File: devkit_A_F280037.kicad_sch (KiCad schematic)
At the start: 4 parts, among them J1 DEVKIT_C2000_ROW_A, J2 DEVKIT_C2000_ROW_B, J3 JTAG_CTBP_10, U1 TMS320F280037CSPM

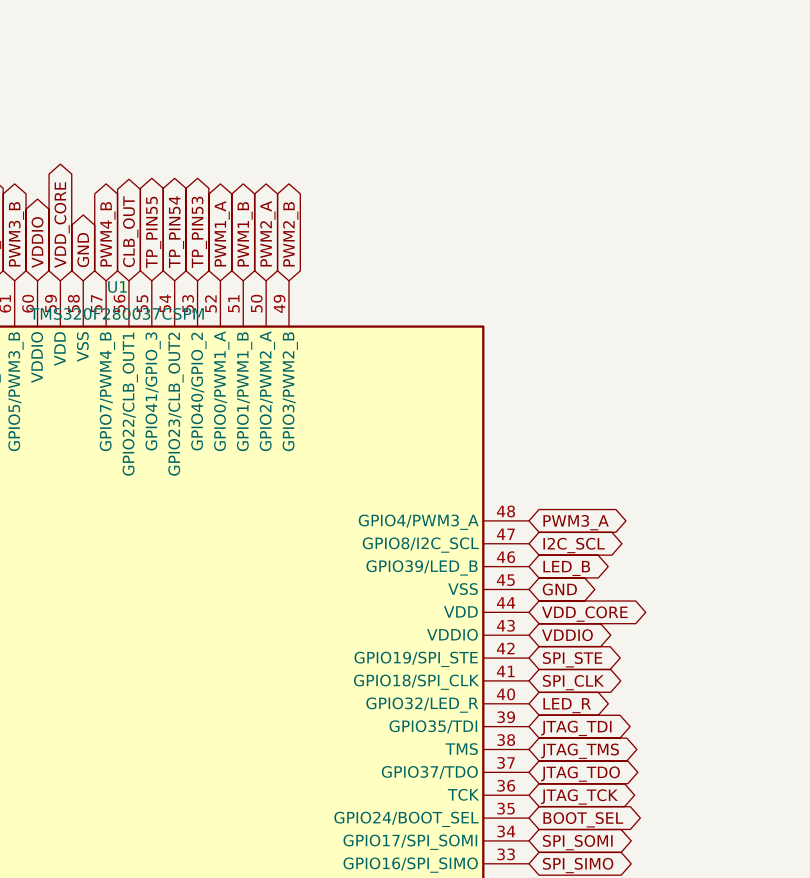
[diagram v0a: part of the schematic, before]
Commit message: LED reportees sur GPIO40 et GPIO23, les deux broches les moins dotees
GPIO32 doit valoir 1 au boot dans les deux modes retenus — Flash (1 1) et SCI
(0 1), ce dernier etant le chemin de mise a jour par l'ESP32. Une LED l'aurait
tenue vers 2,1 V, sous le VIH, cassant les deux d'un coup. GPIO39 part avec.

Broches d'accueil choisies au nombre de fonctions alternatives sacrifiees:
GPIO23 en a 7, GPIO40 en a 9, contre 12 pour GPIO9 qu'on garde libre. Elles
sont communes aux deux boitiers, donc les LED deviennent identiques sur A et B.

Les anciennes positions deviennent des pastilles, differentes par variante:
broches 46 et 40 sur le PCB A, 27 et 28 sur le PCB B.

gen_composants.py est verse au depot mais marque inutilisable: il calcule juste
et produit un fichier que KiCad refuse de charger. Cause isolee a l'insertion
des blocs lib_symbols, reproduite avec un seul Device:R et sans instance.

Co-Authored-By: Claude Opus 5 <noreply@anthropic.com>
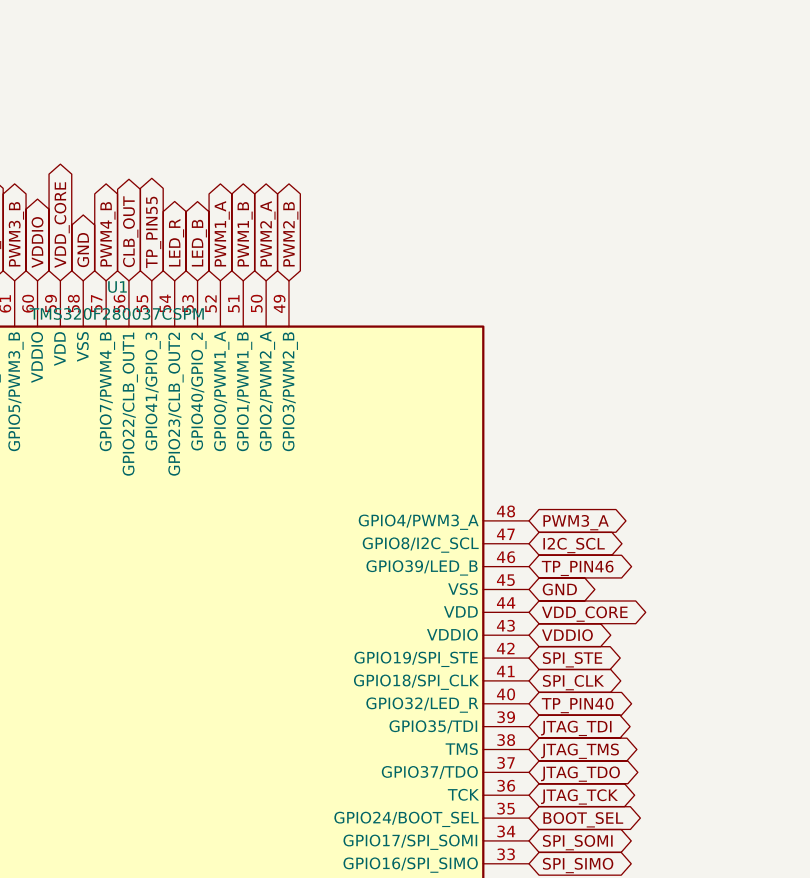
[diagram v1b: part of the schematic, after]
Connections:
- net TP_PIN53 is gone; now on net LED_B: U1.53 (GPIO40/GPIO_2)
- net TP_PIN54 is gone; now on net LED_R: U1.54 (GPIO23/CLB_OUT2)
- net LED_B: no longer U1.46 (GPIO39/LED_B)
- net LED_R: no longer U1.40 (GPIO32/LED_R)
- new net TP_PIN40: U1.40 (GPIO32/LED_R)
- new net TP_PIN46: U1.46 (GPIO39/LED_B)
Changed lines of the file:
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@@
     (effects (font (size 1.27 1.27)) (justify left))
   )
-  (global_label "LED_R" (shape bidirectional) (at 172.72 102.87 0)
+  (global_label "TP_PIN40" (shape bidirectional) (at 172.72 102.87 0)
     (effects (font (size 1.27 1.27)) (justify left))
   )
@@
     (effects (font (size 1.27 1.27)) (justify left))
   )
-  (global_label "LED_B" (shape bidirectional) (at 172.72 87.63 0)
+  (global_label "TP_PIN46" (shape bidirectional) (at 172.72 87.63 0)
     (effects (font (size 1.27 1.27)) (justify left))
   )
@@
     (effects (font (size 1.27 1.27)) (justify left))
   )
-  (global_label "TP_PIN53" (shape bidirectional) (at 135.89 55.88 90)
+  (global_label "LED_B" (shape bidirectional) (at 135.89 55.88 90)
     (effects (font (size 1.27 1.27)) (justify left))
   )
-  (global_label "TP_PIN54" (shape bidirectional) (at 133.35 55.88 90)
+  (global_label "LED_R" (shape bidirectional) (at 133.35 55.88 90)
     (effects (font (size 1.27 1.27)) (justify left))
   )

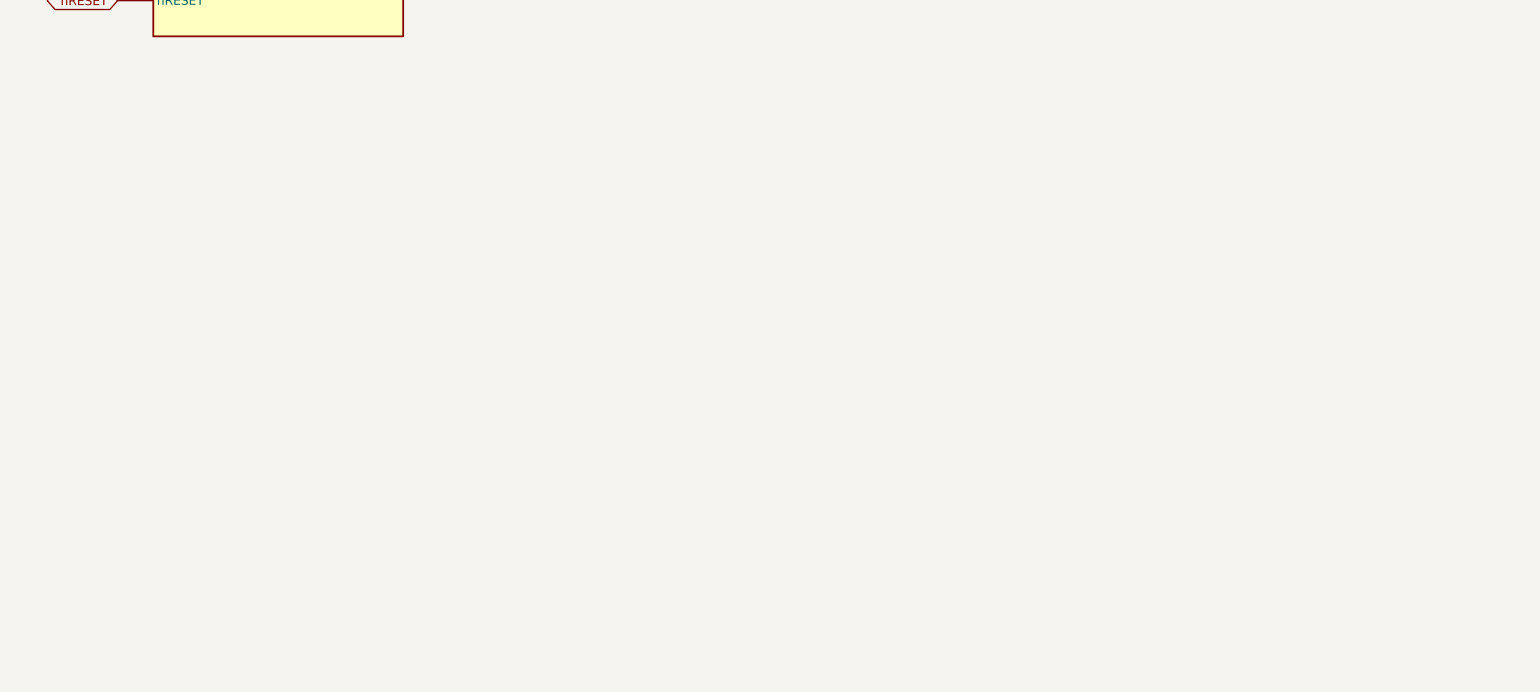
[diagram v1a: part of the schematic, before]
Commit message: Pose les 23 composants dans les deux schemas devkit
Le generateur produisait un fichier que KiCad refusait de charger. Trois
defauts, trouves par bissection puis par diff contre un bloc que KiCad avait
lui-meme ecrit:

1. Dans un schema, seul le symbole de premier niveau porte le prefixe de
   librairie. Ses sous-unites gardent le nom nu — "TC2050_1_1", pas
   "Connector:TC2050_1_1". Les prefixer aussi suffit a rendre le fichier
   illisible, sans autre diagnostic qu'un « echec du chargement ».
2. L'origine de placement n'etait pas un multiple de 1,27 mm: 23 broches hors
   grille, un endpoint_off_grid par composant.
3. Une variante declaree par (extends ...) n'herite que de la geometrie. Sans
   reporter ses propres proprietes sur le bloc de l'ancetre, le symbole pose
   differe de celui que KiCad recalcule et l'ERC leve lib_symbol_mismatch.

ERC apres coup: aucune violation nouvelle sur les deux cartes.

Co-Authored-By: Claude Opus 5 <noreply@anthropic.com>
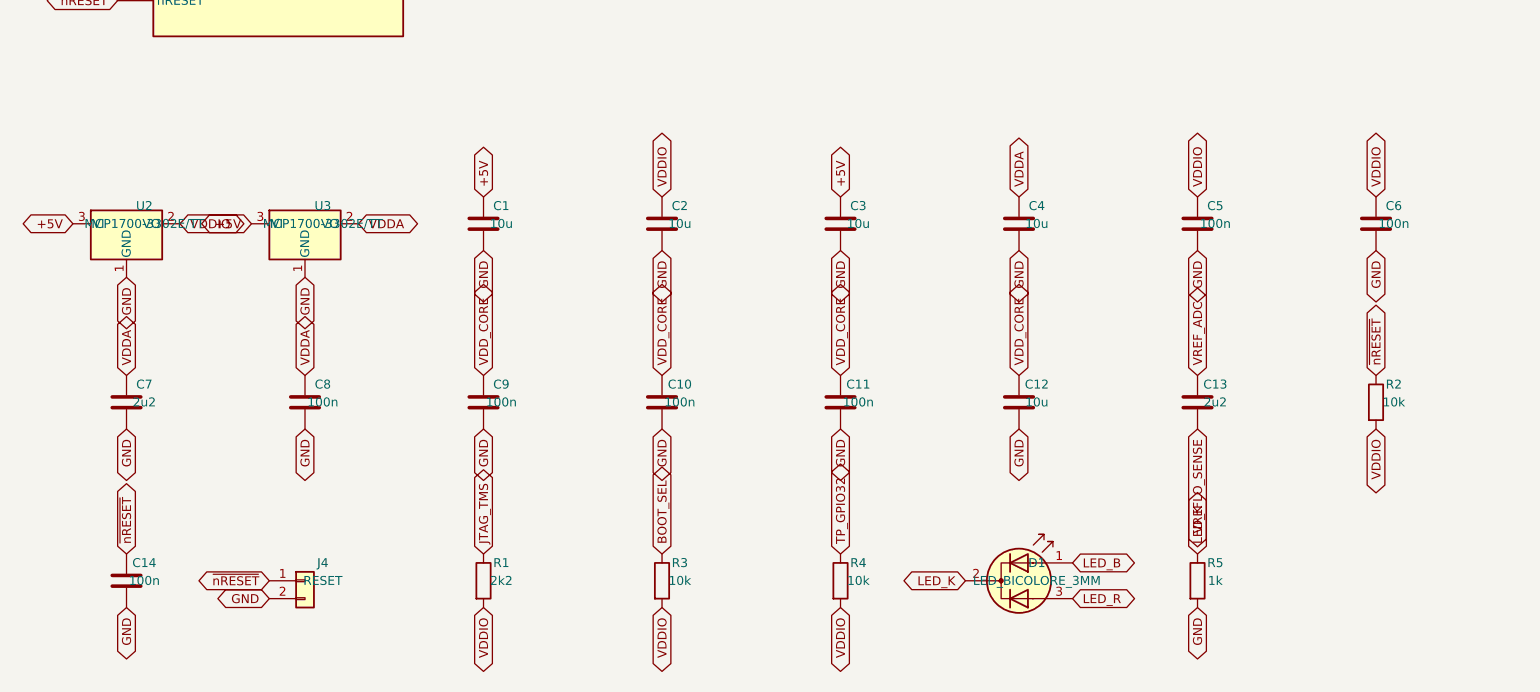
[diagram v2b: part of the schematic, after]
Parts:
- added C1, C12, C2, C3, C4: 10u, Capacitor_SMD:C_0805_2012Metric, symbol Device:C
- added C10, C11, C14, C5, C6, C8, C9: 100n, Capacitor_SMD:C_0805_2012Metric, symbol Device:C
- added C13, C7: 2u2, Capacitor_SMD:C_0805_2012Metric, symbol Device:C
- added D1: LED_BICOLORE_3MM, LED_THT:LED_D3.0mm-3, symbol Device:LED_Dual_AKA
- added J4: RESET, Connector_PinHeader_2.54mm:PinHeader_1x02_P2.54mm_Vertical, symbol Connector_Generic:Conn_01x02
- added R1: 2k2, Resistor_SMD:R_0805_2012Metric, symbol Device:R
- added R2, R3, R4: 10k, Resistor_SMD:R_0805_2012Metric, symbol Device:R
- added R5: 1k, Resistor_SMD:R_0805_2012Metric, symbol Device:R
- added U2, U3: MCP1700-3302E/TT, Package_TO_SOT_SMD:SOT-23, symbol Regulator_Linear:MCP1700x-330xxTT
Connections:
- net +5V: now also C1.1, C3.1, U2.3 (VI), U3.3 (VI)
- net BOOT_SEL: now also R3.1
- net GND: now also C1.2, C10.2, C11.2, C12.2, C14.2, C2.2, C3.2, C4.2, C5.2, C6.2, C7.2, C8.2, C9.2, J4.2 (Pin_2), R5.2, U2.1 (GND), U3.1 (GND)
- net JTAG_TMS: now also R1.1
- net LED_B: now also D1.1 (A1)
- net LED_R: now also D1.3 (A2)
- net VDDA: now also C4.1, C7.1, C8.1, U3.2 (VO)
- net VDDIO: now also C2.1, C5.1, C6.1, R1.2, R2.2, R3.2, R4.2, U2.2 (VO)
- net VDD_CORE: now also C10.1, C11.1, C12.1, C9.1
- net VREFLO_SENSE: now also C13.2
- net VREF_ADC: now also C13.1
- net ~{nRESET}: now also C14.1, J4.1 (Pin_1), R2.1
- new net LED_K: D1.2 (K), R5.1
- new net TP_GPIO32: R4.1

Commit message: Renseigne les empreintes manquantes sur J1, J2, J3 et U1
« Mettre a jour le PCB depuis le schema » a pose 23 empreintes sur 26 et
refuse les trois plus importantes: le MCU et les deux rangees du connecteur.
Cause: KiCad lit la propriete Footprint de l'INSTANCE, pas celle de la
librairie, et les schemas importes la portaient vide — ou pas du tout.

Les deux formats coexistent dans le depot et demandaient deux traitements:
KiCad 10 ecrit une propriete Footprint vide qu'il suffit de remplir, KiCad 8
n'en ecrit aucune et il faut l'inserer.

Le cache (lib_symbols) du schema n'etait pas une source fiable non plus:
plusieurs symboles y avaient perdu leur empreinte alors que la librairie la
porte. gen_empreintes.py lit donc sym-lib-table et fait primer la librairie.

ERC inchange sur les deux cartes.

Co-Authored-By: Claude Opus 5 <noreply@anthropic.com>
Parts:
- J1, J2: footprint (none) -> Connector_PinHeader_2.54mm:PinHeader_1x28_P2.54mm_Vertical
- J3: footprint (none) -> Connector_PinHeader_1.27mm:PinHeader_2x05_P1.27mm_Vertical
- U1: footprint (none) -> Package_QFP:LQFP-64_10x10mm_P0.5mm
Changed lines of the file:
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@@
     (property "Reference" "U1" (at 127 56.6 0) (effects (font (size 1.27 1.27))))
     (property "Value" "TMS320F280037CSPM" (at 127 59.6 0) (effects (font (size 1.27 1.27))))
+    (property "Footprint" "Package_QFP:LQFP-64_10x10mm_P0.5mm" (at 0 0 0) (effects (font (size 1.27 1.27)) (hide yes)))
     (pin "6")
     (pin "7")
@@
     (property "Reference" "J1" (at 279.4 14.69 0) (effects (font (size 1.27 1.27))))
     (property "Value" "DEVKIT_C2000_ROW_A" (at 279.4 17.69 0) (effects (font (size 1.27 1.27))))
+    (property "Footprint" "Connector_PinHeader_2.54mm:PinHeader_1x28_P2.54mm_Vertical" (at 0 0 0) (effects (font (size 1.27 1.27)) (hide yes)))
     (pin "1")
     (pin "2")
@@
     (property "Reference" "J2" (at 279.4 115.02 0) (effects (font (size 1.27 1.27))))
     (property "Value" "DEVKIT_C2000_ROW_B" (at 279.4 118.02 0) (effects (font (size 1.27 1.27))))
+    (property "Footprint" "Connector_PinHeader_2.54mm:PinHeader_1x28_P2.54mm_Vertical" (at 0 0 0) (effects (font (size 1.27 1.27)) (hide yes)))
     (pin "1")
     (pin "2")
@@
     (property "Reference" "J3" (at 59.69 154.39 0) (effects (font (size 1.27 1.27))))
     (property "Value" "JTAG_CTBP_10" (at 59.69 157.39 0) (effects (font (size 1.27 1.27))))
+    (property "Footprint" "Connector_PinHeader_1.27mm:PinHeader_2x05_P1.27mm_Vertical" (at 0 0 0) (effects (font (size 1.27 1.27)) (hide yes)))
     (pin "1")
     (pin "2")

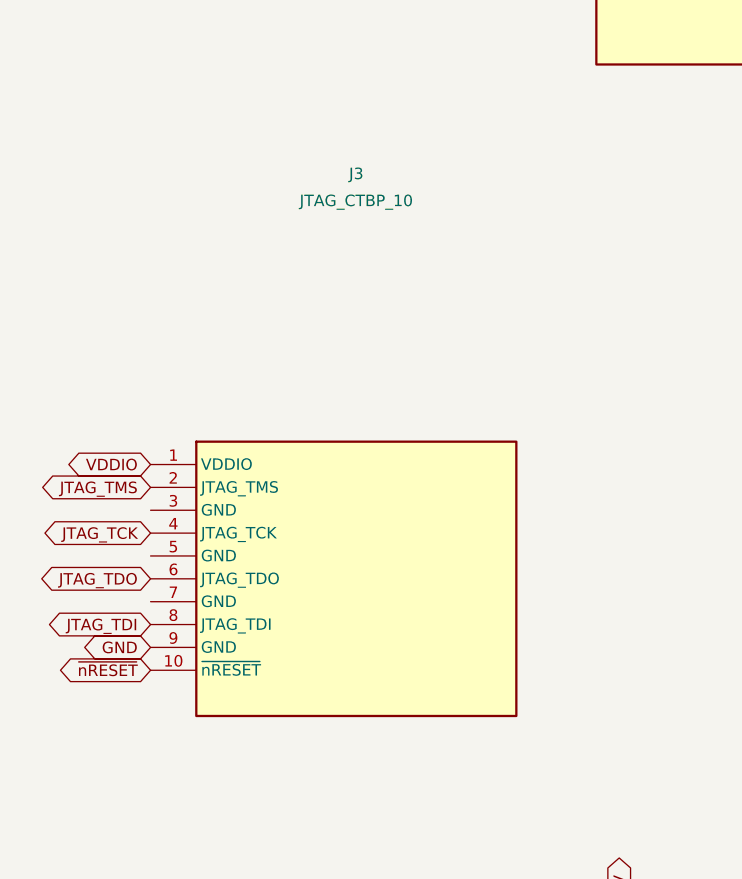
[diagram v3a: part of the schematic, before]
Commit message: Devkit A: embase cTBP 10 points remplacee par le Tag-Connect TC2050
La specification etait passee au TC2050 et le devkit B l'avait recu a la main,
mais le A portait encore l'ancienne embase au pas 1,27 mm. Les deux cartes
doivent avoir les memes composants.

Le brochage repris est celui, releve et verifie, du devkit B — le standard TI
10 points: 1 GND, 2 TCK, 3 TDO, 4 TMS, 5 TDI, 7 nRESET, 10 VDDIO. Les broches
6, 8 et 9 restent libres: ce composant n'a pas de TRSTn (SPRSPC5 section 5.3),
c'est le rappel de 2,2 kOhms sur TMS qui en tient lieu.

Le symbole JTAG_CTBP_10 et ses etiquettes sont retires, et sa definition avec
puisque plus personne ne l'utilise.

ERC: les deux cartes convergent, 14 power_pin_not_driven de chaque cote contre
17 sur le A auparavant. Les 27 instances portent leur empreinte, le F8 peut
etre lance.

Co-Authored-By: Claude Opus 5 <noreply@anthropic.com>
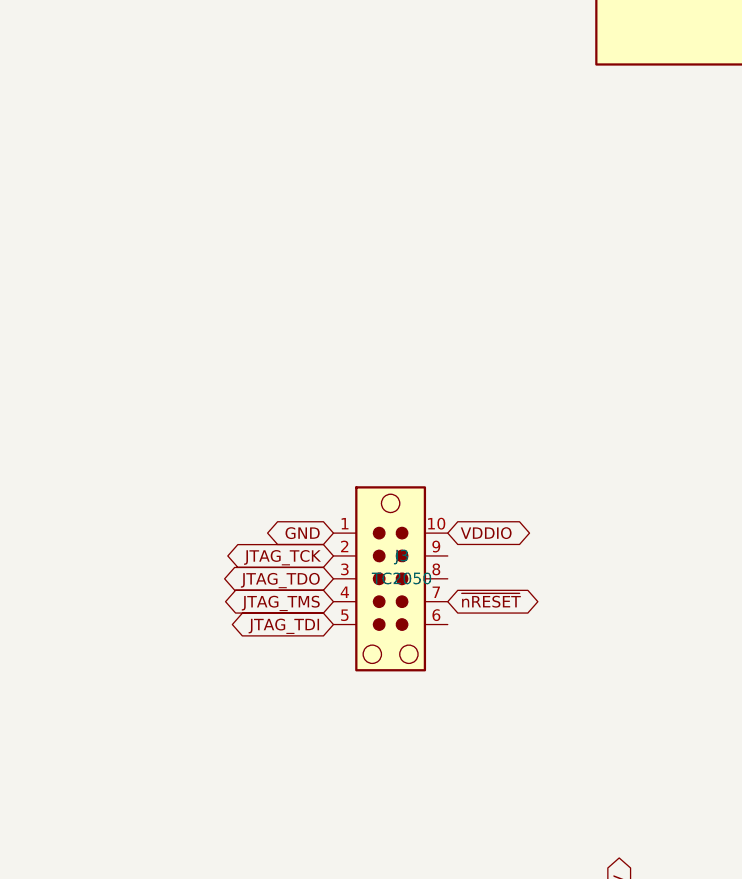
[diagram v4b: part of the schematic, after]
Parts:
- removed J3: JTAG_CTBP_10, Connector_PinHeader_1.27mm:PinHeader_2x05_P1.27mm_Vertical, symbol C2000_Devkit_Connectors:JTAG_CTBP_10
- added J3: TC2050, Connector:Tag-Connect_TC2050-IDC-NL_2x05_P1.27mm_Vertical, symbol Connector:TC2050
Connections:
- net GND: now also J3.1
- net JTAG_TCK: now also J3.2
- net JTAG_TDI: now also J3.5
- net JTAG_TDO: now also J3.3
- net JTAG_TMS: now also J3.4
- net VDDIO: now also J3.10
- net ~{nRESET}: now also J3.7
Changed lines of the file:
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@@
     (instances (project "devkit_A_F280037" (path "/b862ab70-d3e9-7521-c4b2-1a1fcce3c7bb" (reference "J2") (unit 1))))
   )
-  (symbol (lib_id "C2000_Devkit_Connectors:JTAG_CTBP_10") (at 59.69 199.39 0) (unit 1)
-    (exclude_from_sim no) (in_bom yes) (on_board yes) (dnp no)
-    (property "Reference" "J3" (at 59.69 154.39 0) (effects (font (size 1.27 1.27))))
-    (property "Value" "JTAG_CTBP_10" (at 59.69 157.39 0) (effects (font (size 1.27 1.27))))
-    (property "Footprint" "Connector_PinHeader_1.27mm:PinHeader_2x05_P1.27mm_Vertical" (at 0 0 0) (effects (font (size 1.27 1.27)) (hide yes)))
-    (pin "1")
-    (pin "2")
-    (pin "3")
-    (pin "4")
-    (pin "5")
-    (pin "6")
-    (pin "7")
-    (pin "8")
-    (pin "9")
-    (pin "10")
-    (instances (project "devkit_A_F280037" (path "/b862ab70-d3e9-7521-c4b2-1a1fcce3c7bb" (reference "J3") (unit 1))))
-  )
   (global_label "Vin" (shape bidirectional) (at 81.28 95.25 180)
     (effects (font (size 1.27 1.27)) (justify right))
@@
   )
   (global_label "GPIO_1" (shape bidirectional) (at 256.54 193.04 180)
-    (effects (font (size 1.27 1.27)) (justify right))
-  )
-  (global_label "VDDIO" (shape bidirectional) (at 36.83 186.69 180)
-    (effects (font (size 1.27 1.27)) (justify right))
-  )
-  (global_label "JTAG_TMS" (shape bidirectional) (at 36.83 189.23 180)
-    (effects (font (size 1.27 1.27)) (justify right))
-  )
-  (global_label "JTAG_TCK" (shape bidirectional) (at 36.83 194.31 180)
-    (effects (font (size 1.27 1.27)) (justify right))
-  )
-  (global_label "JTAG_TDO" (shape bidirectional) (at 36.83 199.39 180)
-    (effects (font (size 1.27 1.27)) (justify right))
-  )
-  (global_label "JTAG_TDI" (shape bidirectional) (at 36.83 204.47 180)
-    (effects (font (size 1.27 1.27)) (justify right))
-  )
-  (global_label "GND" (shape bidirectional) (at 36.83 207.01 180)
-    (effects (font (size 1.27 1.27)) (justify right))
-  )
-  (global_label "~{nRESET}" (shape bidirectional) (at 36.83 209.55 180)
     (effects (font (size 1.27 1.27)) (justify right))
   )
@@
 		(effects (font (size 1.27 1.27)) (justify right))
 	)
+	(symbol (lib_id "Connector:TC2050") (at 62.23 199.39 0) (unit 1)
+		(exclude_from_sim no) (in_bom yes) (on_board yes) (dnp no)
+		(property "Reference" "J3" (at 64.77 196.85 0) (effects (font (size 1.27 1.27))))
+		(property "Value" "TC2050" (at 64.77 199.39 0) (effects (font (size 1.27 1.27))))
+		(property "Footprint" "Connector:Tag-Connect_TC2050-IDC-NL_2x05_P1.27mm_Vertical" (at 62.23 199.39 0) (effects (font (size 1.27 1.27)) (hide yes)))
+		(pin "1")
+		(pin "2")
+		(pin "3")
+		(pin "4")
+		(pin "5")
+		(pin "6")
+		(pin "7")
+		(pin "8")
+		(pin "9")
+		(pin "10")
+		(instances
+			(project "devkit_A_F280037"
+				(path "/cc085941-203a-19c6-3985-50f005d3074a" (reference "J3") (unit 1))
+			)
+		)
+	)
+	(global_label "GND" (shape bidirectional) (at 57.15 194.31 180)
+		(effects (font (size 1.27 1.27)) (justify right))
+	)
+	(global_label "JTAG_TCK" (shape bidirectional) (at 57.15 196.85 180)
+		(effects (font (size 1.27 1.27)) (justify right))
+	)
+	(global_label "JTAG_TDO" (shape bidirectional) (at 57.15 199.39 180)
+		(effects (font (size 1.27 1.27)) (justify right))
+	)
+	(global_label "JTAG_TMS" (shape bidirectional) (at 57.15 201.93 180)
+		(effects (font (size 1.27 1.27)) (justify right))
+	)
+	(global_label "JTAG_TDI" (shape bidirectional) (at 57.15 204.47 180)
+		(effects (font (size 1.27 1.27)) (justify right))
+	)
+	(global_label "~{nRESET}" (shape bidirectional) (at 69.85 201.93 0)
+		(effects (font (size 1.27 1.27)) (justify left))
+	)
+	(global_label "VDDIO" (shape bidirectional) (at 69.85 194.31 0)
+		(effects (font (size 1.27 1.27)) (justify left))
+	)
 )
